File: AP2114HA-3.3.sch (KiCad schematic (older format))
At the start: 3 parts

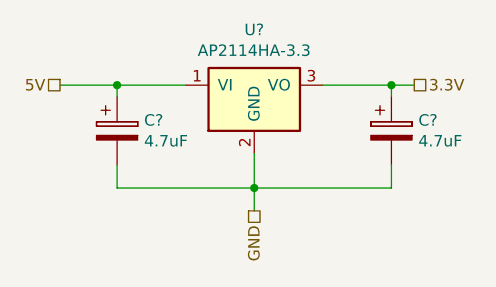
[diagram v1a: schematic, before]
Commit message: Annotated schematic and added footprints.
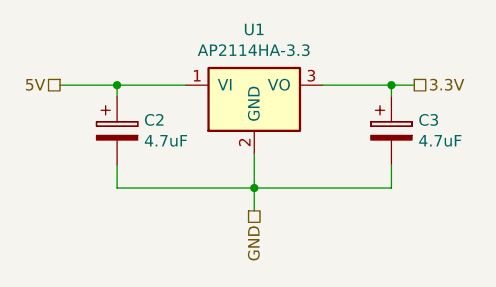
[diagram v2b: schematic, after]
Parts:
- C2, C3: renamed from C?; footprint (none) -> Capacitors_THT:CP_Radial_D5.0mm_P2.50mm
- U1: renamed from U?; footprint (none) -> TO_SOT_Packages_SMD:SOT-223
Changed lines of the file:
@@
 AR Path="/5BD8A06D" Ref="U?"  Part="1"
 AR Path="/5BD89DA4/5BD8A06D" Ref="U?"  Part="1"
-AR Path="/5BD89B2B/5BD8A06D" Ref="U?"  Part="1"
-F 0 "U?" H 5150 3492 50  0000 C CNN
+AR Path="/5BD89B2B/5BD8A06D" Ref="U1"  Part="1"
+F 0 "U1" H 5150 3492 50  0000 C CNN
 F 1 "AP2114HA-3.3" H 5150 3401 50  0000 C CNN
-F 2 "" H 5200 3650 50  0001 C CNN
+F 2 "TO_SOT_Packages_SMD:SOT-223" H 5200 3650 50  0001 C CNN
 F 3 "" H 5200 3650 50  0001 C CNN
 	1    5150 3200
@@
 GND
 $Comp
-L Device:CP C?
+L Device:CP C2
 U 1 1 5BD8DE35
 P 4550 3350
-F 0 "C?" H 4668 3396 50  0000 L CNN
+F 0 "C2" H 4668 3396 50  0000 L CNN
 F 1 "4.7uF" H 4668 3305 50  0000 L CNN
-F 2 "" H 4588 3200 50  0001 C CNN
+F 2 "Capacitors_THT:CP_Radial_D5.0mm_P2.50mm" H 4588 3200 50  0001 C CNN
 F 3 "~" H 4550 3350 50  0001 C CNN
 	1    4550 3350
@@
 $EndComp
 $Comp
-L Device:CP C?
+L Device:CP C3
 U 1 1 5BD8E00D
 P 5750 3350
-F 0 "C?" H 5868 3396 50  0000 L CNN
+F 0 "C3" H 5868 3396 50  0000 L CNN
 F 1 "4.7uF" H 5868 3305 50  0000 L CNN
-F 2 "" H 5788 3200 50  0001 C CNN
+F 2 "Capacitors_THT:CP_Radial_D5.0mm_P2.50mm" H 5788 3200 50  0001 C CNN
 F 3 "~" H 5750 3350 50  0001 C CNN
 	1    5750 3350
